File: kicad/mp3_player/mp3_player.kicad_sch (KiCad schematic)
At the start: 18 parts, among them SW1 Boot, SW2 Reset, SW3 RotaryEncoder_Switch, U1 MPU6500-breakout, U2 HC-SR04_Ultrasonic_Sensor, U3 ESP32-S3-WROOM-1, U4 AHT20_BMP280

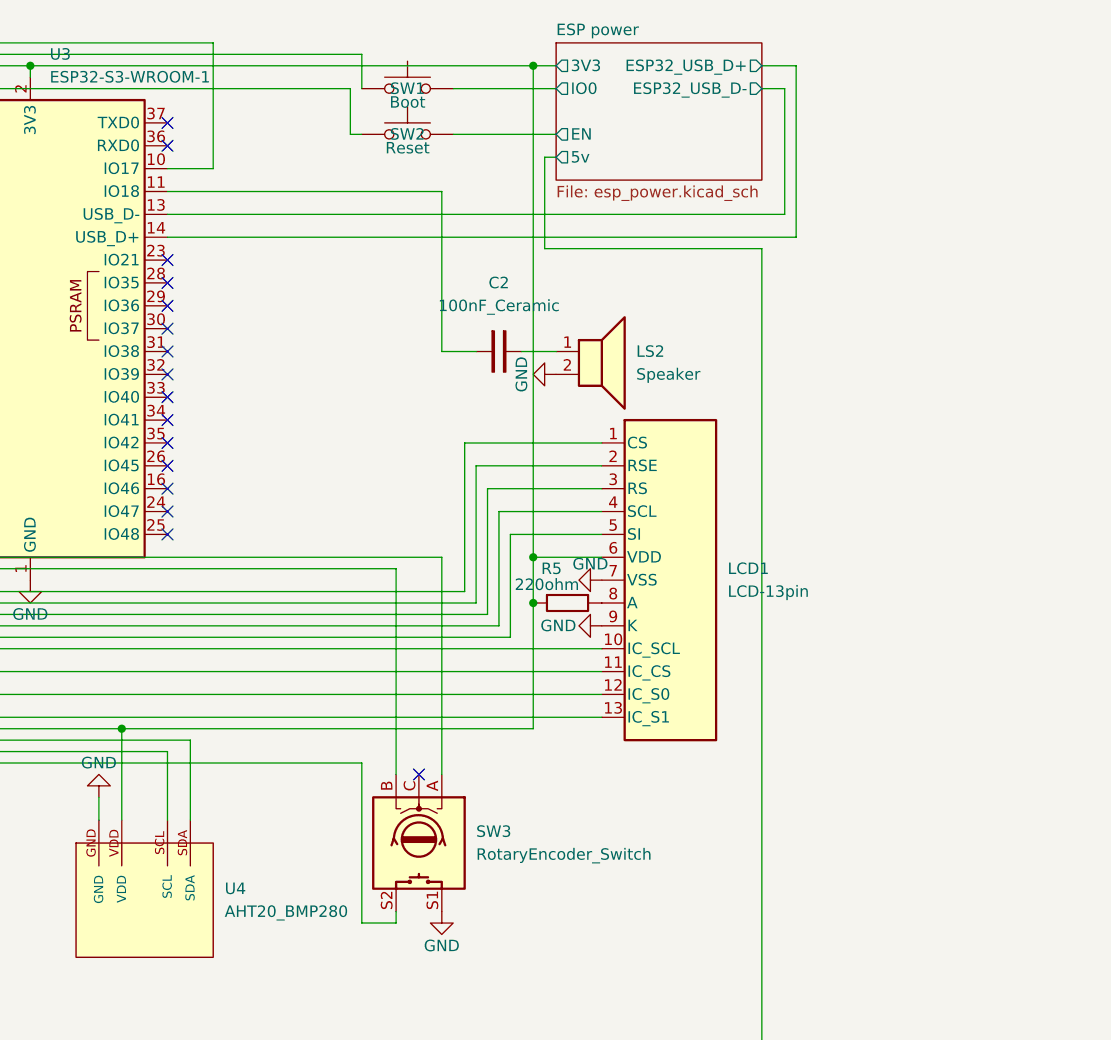
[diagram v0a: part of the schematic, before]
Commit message: [ADD] an initial set of libraries to depressed to do their own job
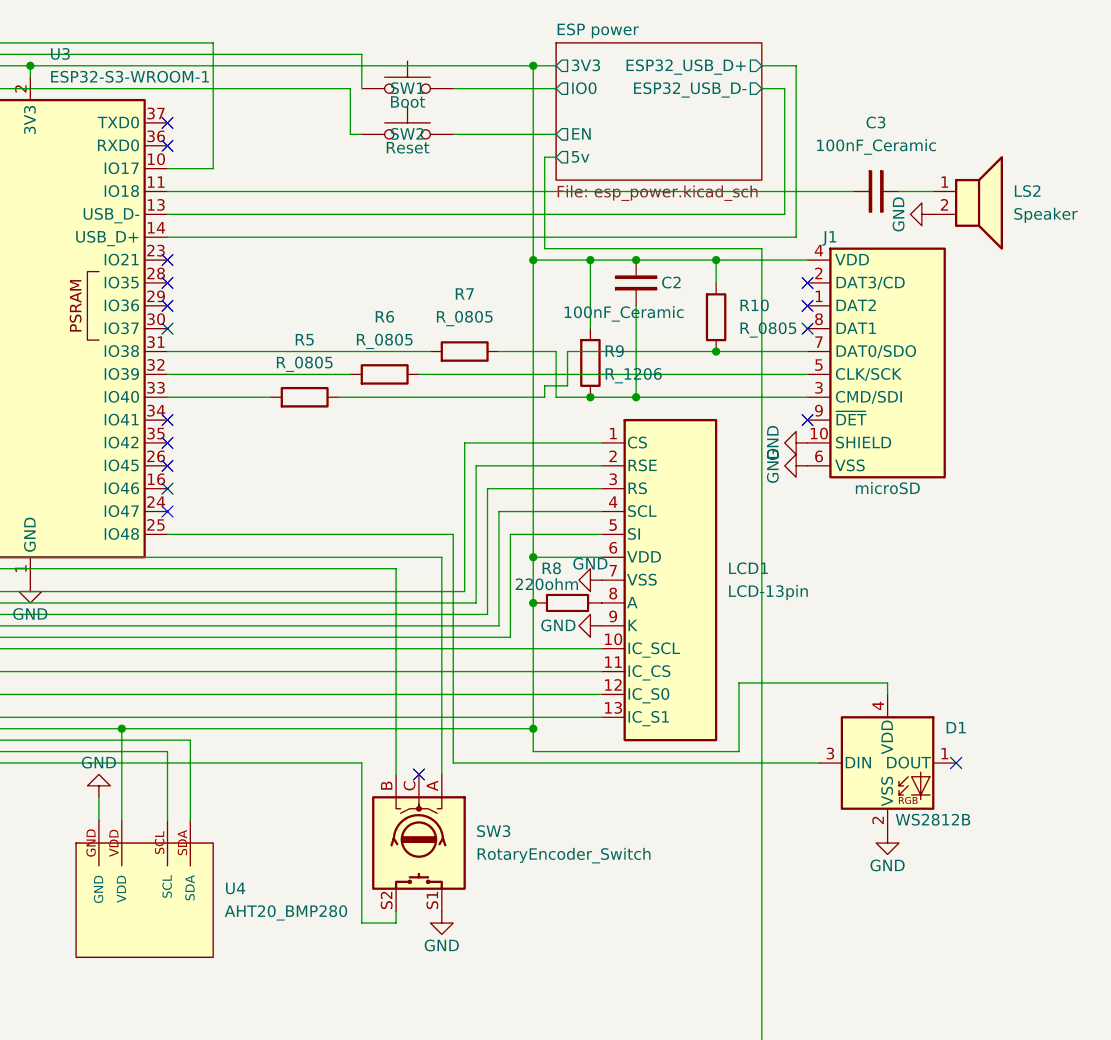
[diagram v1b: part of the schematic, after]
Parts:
- added C2: 100nF_Ceramic, Capacitor_THT:C_Disc_D5.0mm_W2.5mm_P2.50mm, symbol PCM_SL_Capacitors:100nF_Ceramic
- added D1: WS2812B, PCM_SparkFun-LED:WS2812_2020, symbol PCM_SparkFun-LED:WS2812B_2020
- added J1: microSD, PCM_SparkFun-Connector:microSD_External_Pin, symbol PCM_SparkFun-Connector:microSD_PushPush
- added R10, R5, R6, R7: R_0805, PCM_Resistor_SMD_AKL:R_0805_2012Metric, symbol PCM_Resistor_AKL:R_0805
- added R9: R_1206, PCM_Resistor_SMD_AKL:R_1206_3216Metric, symbol PCM_Resistor_AKL:R_1206
- renumbered C2 to C3, R5 to R8
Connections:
- net ESP power/3V3: now also C2.2, D1.4 (VDD), J1.4 (VDD), R10.1, R9.1
- net GND: now also D1.2 (VSS), J1.10 (SHIELD), J1.6 (VSS)
- net at U3.25 (IO48): now also D1.3 (DIN)
- net at U3.31 (IO38): now also R7.1
- net at U3.32 (IO39): now also R6.1
- net at U3.33 (IO40): now also R5.1
- new net: C2.1, J1.3 (CMD/SDI), R7.2, R9.2
- new net: J1.5 (CLK/SCK), R6.2
- new net: J1.7 (DAT0/SDO), R10.2, R5.2
- no-connect marks 19 -> 20
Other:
- moved on the sheet: C3, LS2

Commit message: [FIX] issues where lines SCL and SDA were crossed on the schematic
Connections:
- net at R4.1, U1.4 (SDA), U1.5 (EDA)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: now also U4.SDA; no longer U4.SCL
- net at R3.1, U1.3 (SCL), U1.6 (ECL)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: now also U4.SCL; no longer U4.SDA
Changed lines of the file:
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@@
-	)
-	(junction
-		(at 44.45 91.44)
-		(diameter 0)
-		(color 0 0 0 0)
-	)
-	(junction
-		(at 45.72 92.71)
-		(diameter 0)
-		(color 0 0 0 0)
 	)
 	(junction
@@
 	)
 	(junction
+		(at 44.45 92.71)
+		(diameter 0)
+		(color 0 0 0 0)
+	)
+	(junction
 		(at 133.35 16.51)
 		(diameter 0)
@@
 		(color 0 0 0 0)
 	)
+	(junction
+		(at 45.72 91.44)
+		(diameter 0)
+		(color 0 0 0 0)
+	)
 	(no_connect
 		(at 148.59 58.42)
@@
 	(wire
 		(pts
+			(xy 45.72 91.44) (xy 45.72 105.41)
+		)
+		(stroke
+			(width 0)
+			(type default)
+		)
+	)
+	(wire
+		(pts
 			(xy 212.09 85.09) (xy 212.09 92.71)
 		)
@@
 	(wire
 		(pts
-			(xy 44.45 30.48) (xy 44.45 91.44)
-		)
-		(stroke
-			(width 0)
-			(type default)
-		)
-	)
-	(wire
-		(pts
 			(xy 143.51 90.17) (xy 143.51 100.33)
 		)
@@
 	(wire
 		(pts
+			(xy 45.72 33.02) (xy 45.72 91.44)
+		)
+		(stroke
+			(width 0)
+			(type default)
+		)
+	)
+	(wire
+		(pts
 			(xy 151.13 100.33) (xy 151.13 91.44)
 		)
@@
 	(wire
 		(pts
-			(xy 151.13 91.44) (xy 44.45 91.44)
-		)
-		(stroke
-			(width 0)
-			(type default)
-		)
-	)
-	(wire
-		(pts
 			(xy 52.07 48.26) (xy 55.88 48.26)
 		)
@@
 	(wire
 		(pts
-			(xy 44.45 91.44) (xy 44.45 102.87)
+			(xy 44.45 30.48) (xy 44.45 92.71)
 		)
 		(stroke
@@
 	(wire
 		(pts
+			(xy 151.13 91.44) (xy 45.72 91.44)
+		)
+		(stroke
+			(width 0)
+			(type default)
+		)
+	)
+	(wire
+		(pts
 			(xy 185.42 66.04) (xy 196.85 66.04)
 		)
@@
 	(wire
 		(pts
+			(xy 44.45 92.71) (xy 44.45 102.87)
+		)
+		(stroke
+			(width 0)
+			(type default)
+		)
+	)
+	(wire
+		(pts
 			(xy 114.3 15.24) (xy 114.3 27.94)
 		)
@@
 	(wire
 		(pts
-			(xy 45.72 92.71) (xy 45.72 105.41)
-		)
-		(stroke
-			(width 0)
-			(type default)
-		)
-	)
-	(wire
-		(pts
 			(xy 44.45 110.49) (xy 46.99 110.49)
 		)
@@
 	(wire
 		(pts
-			(xy 45.72 92.71) (xy 148.59 92.71)
-		)
-		(stroke
-			(width 0)
-			(type default)
-		)
-	)
-	(wire
-		(pts
 			(xy 45.72 33.02) (xy 102.87 33.02)
 		)
@@
 	(wire
 		(pts
-			(xy 45.72 33.02) (xy 45.72 92.71)
-		)
-		(stroke
+			(xy 44.45 92.71) (xy 148.59 92.71)
+		)
+		(stroke

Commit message: [UPDATE] the circuit connections to match the current implementation
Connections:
- net at LED1.2 (DIN): now also U3.34 (IO41); no longer U3.15 (IO3)
- net at U3.35 (IO42): now also SW3.A
- net at U3.9 (IO16): no longer SW3.A
- no-connect marks 20 -> 19
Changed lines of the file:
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@@
-	)
-	(no_connect
-		(at 148.59 58.42)
 	)
 	(no_connect
@@
 	)
 	(no_connect
+		(at 118.11 68.58)
+	)
+	(no_connect
 		(at 148.59 45.72)
 	)
@@
 	)
 	(no_connect
-		(at 148.59 55.88)
-	)
-	(no_connect
 		(at 55.88 140.97)
 	)
@@
 	(wire
 		(pts
-			(xy 179.07 71.12) (xy 116.84 71.12)
-		)
-		(stroke
-			(width 0)
-			(type default)
-		)
-	)
-	(wire
-		(pts
 			(xy 170.18 93.98) (xy 170.18 111.76)
 		)
@@
 	(wire
 		(pts
+			(xy 36.83 12.7) (xy 154.94 12.7)
+		)
+		(stroke
+			(width 0)
+			(type default)
+		)
+	)
+	(wire
+		(pts
 			(xy 76.2 60.96) (xy 77.47 60.96)
 		)
@@
 	(wire
 		(pts
+			(xy 148.59 55.88) (xy 154.94 55.88)
+		)
+		(stroke
+			(width 0)
+			(type default)
+		)
+	)
+	(wire
+		(pts
 			(xy 100.33 16.51) (xy 100.33 22.86)
 		)
@@
 	(wire
 		(pts
-			(xy 116.84 71.12) (xy 116.84 68.58)
-		)
-		(stroke
-			(width 0)
-			(type default)
-		)
-	)
-	(wire
-		(pts
 			(xy 45.72 33.02) (xy 45.72 91.44)
 		)
@@
 	(wire
 		(pts
+			(xy 153.67 13.97) (xy 153.67 27.94)
+		)
+		(stroke
+			(width 0)
+			(type default)
+		)
+	)
+	(wire
+		(pts
 			(xy 151.13 100.33) (xy 151.13 91.44)
 		)
@@
 	(wire
 		(pts
+			(xy 148.59 58.42) (xy 179.07 58.42)
+		)
+		(stroke
+			(width 0)
+			(type default)
+		)
+	)
+	(wire
+		(pts
+			(xy 154.94 55.88) (xy 154.94 12.7)
+		)
+		(stroke
+			(width 0)
+			(type default)
+		)
+	)
+	(wire
+		(pts
 			(xy 189.23 92.71) (xy 189.23 90.17)
 		)
@@
 	(wire
 		(pts
-			(xy 153.67 13.97) (xy 153.67 27.94)
-		)
-		(stroke
-			(width 0)
-			(type default)
-		)
-	)
-	(wire
-		(pts
 			(xy 193.04 48.26) (xy 209.55 48.26)
 		)
@@
 	(wire
 		(pts
-			(xy 116.84 68.58) (xy 118.11 68.58)
-		)
-		(stroke
-			(width 0)
-			(type default)
-		)
-	)
-	(wire
-		(pts
 			(xy 105.41 74.93) (xy 105.41 53.34)
 		)
@@
 	(wire
 		(pts
-			(xy 179.07 71.12) (xy 179.07 95.25)
+			(xy 179.07 58.42) (xy 179.07 95.25)
 		)
 		(stroke
@@
 	(wire
 		(pts
-			(xy 36.83 35.56) (xy 36.83 121.92)
+			(xy 36.83 12.7) (xy 36.83 121.92)
 		)
 		(stroke
@@
 		)
 		(stroke
-			(width 0)
-			(type default)
-		)
-	)
-	(wire
-		(pts
-			(xy 36.83 35.56) (xy 118.11 35.56)
-		)
-		(stroke
